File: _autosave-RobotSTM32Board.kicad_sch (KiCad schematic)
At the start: 74 parts, among them IC1 TB6612FNG, IC2 TB6612FNG, J1 MotorA, J10 Qwiik1, J11 Qwiik2, J12 Qwiik3, J13 Qwiik4, J14 Qwiik5, J2 MotorB, J3 MotorC, J4 MotorD, J5 EncoderA, J6 EncoderB, J7 EncoderC, J8 EncoderD, J9 ESTOP, Q1 NPN, Q2 NMOS_Substrate, Q3 NMOS_Substrate, U1 NUCLEO-F411RE, U3 TPS564252DRLR, U4 TPS51386RJNR, U5 LM27403SQ/NOPB

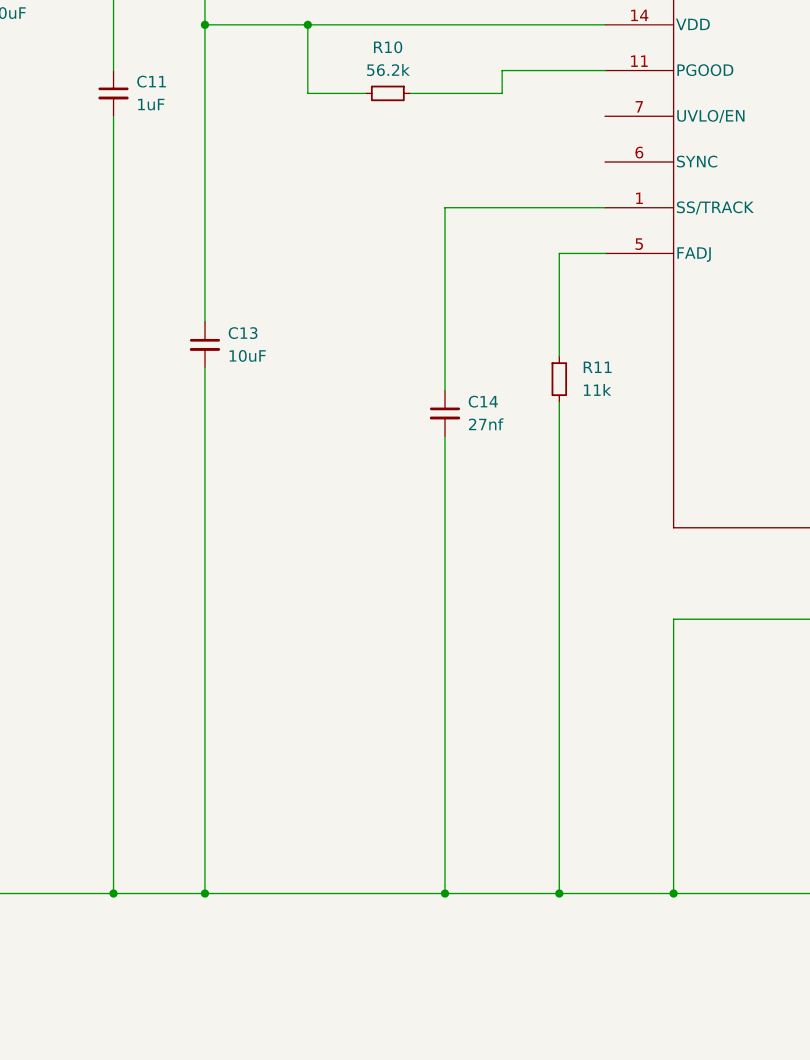
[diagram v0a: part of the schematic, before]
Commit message: corrected buck converters
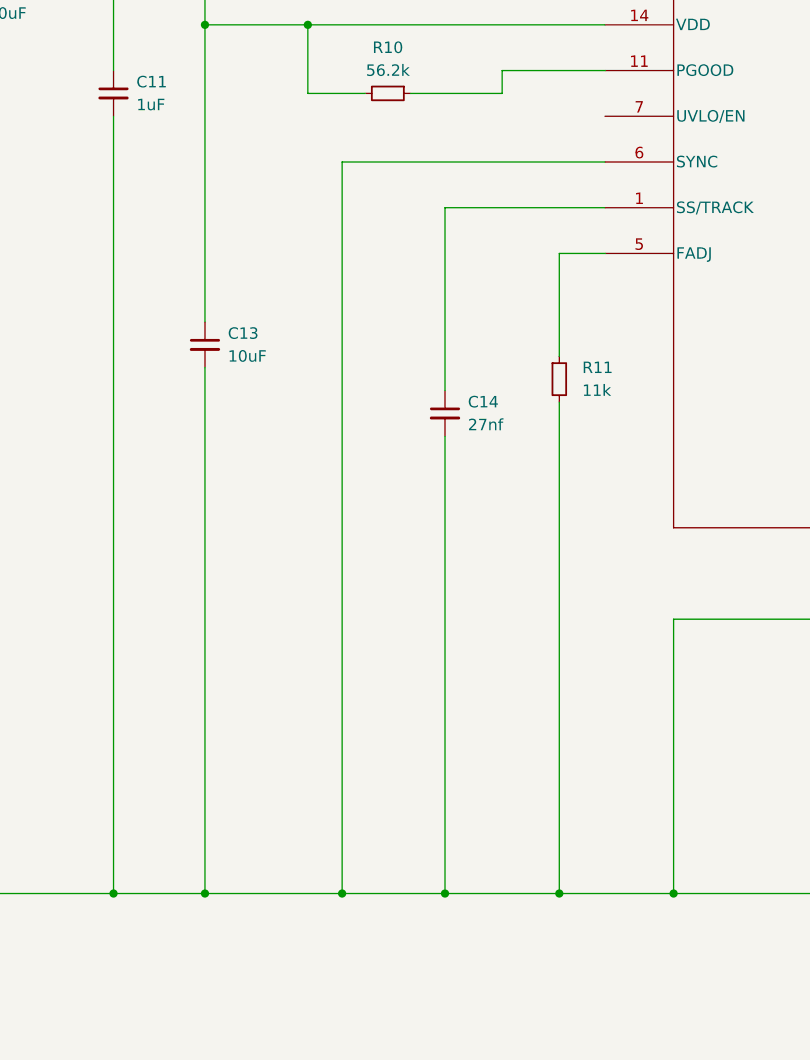
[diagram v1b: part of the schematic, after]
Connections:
- net GND: now also U5.6 (SYNC)
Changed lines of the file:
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@@
+	)
+	(junction
+		(at 396.24 173.99)
+		(diameter 0)
+		(color 0 0 0 0)
 	)
 	(junction
@@
 	(wire
 		(pts
+			(xy 425.45 92.71) (xy 396.24 92.71)
+		)
+		(stroke
+			(width 0)
+			(type default)
+		)
+	)
+	(wire
+		(pts
 			(xy 25.4 21.59) (xy 25.4 25.4)
 		)
@@
 	(wire
 		(pts
-			(xy 381 173.99) (xy 407.67 173.99)
+			(xy 381 173.99) (xy 396.24 173.99)
 		)
 		(stroke
@@
 	(wire
 		(pts
+			(xy 396.24 92.71) (xy 396.24 173.99)
+		)
+		(stroke
+			(width 0)
+			(type default)
+		)
+	)
+	(wire
+		(pts
 			(xy 162.56 229.87) (xy 195.58 229.87)
 		)
@@
 		)
 		(stroke
+			(width 0)
+			(type default)
+		)
+	)
+	(wire
+		(pts
+			(xy 396.24 173.99) (xy 407.67 173.99)
+		)
+		(stroke
